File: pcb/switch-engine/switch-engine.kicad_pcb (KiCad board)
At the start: 10 copper layers, 135 x 111 mm, 369 parts, among them J1 CONN_PCIE_PWR_8PIN, J10 CORTEX_DEBUG_ETM, J11 SMPM, J12 CONN_01X03, J13 PMOD_HOST, J14 ARF6-08-S-D-A-K-TR, J15 ARF6-08-S-D-A-K-TR, J16 CONN_01X10, J17 ARF6-08-S-D-A-K-TR, J18 ARF6-08-S-D-A-K-TR, J19 CONN_01X10, J2 CONN_IBC_MGMT, J20 0826-1G1T-23-F, J21 ARF6-08-S-D-A-K-TR, J22 ARF6-08-S-D-A-K-TR, J23 CONN_01X10, J24 SMPM, J26 RJ45, J3 CONN_01X03, J4 CORTEX_DEBUG_ETM, J5 FAN_01, J6 FAN_01, J7 JUMPER_0402, J8 XILINX_JTAG, J9 PMOD_HOST, M1 SCREWHOLE, M2 SCREWHOLE, M3 SCREWHOLE, M4 SCREWHOLE, M5 LOGO, M6 LOGO, M7 LOGO, M8 960-27-23-D-AB-0, M9 FAN, Q2 SSM6N58NU, SW1 SWITCH, SW2 SWITCH, U1 STM32L431-QFN48, U10 74LVC1T45, U11 74LVC1T45, U12 74LVC1T45, U13 MT25QU256ABA8E12-0AUT, U14 ECS-1612MV-250-CN, U15 SIT9121AI-2BF-XXS156.250000G, U17 AT24MAC402, U18 74LVC1T45, U19 74LVC1T45, U2 MYMGK1R812ERSR, U20 74LVC1T45, U21 74LVC1T45, U22 ECS-1612MV-250-CN, U23 KSZ9031RN, U24 ESD224DQAR, U25 SIT9121AI-2BF-XXS156.250000G, U26 ESD224DQAR, U27 SIT9121AI-2BF-XXS156.250000G, U28 ADP1740ACPZ-2.5-R7, U29 ADM3101E_QFN, U3 MYMGK1R812ERSR, U4 MYMGK00506ERSR, U5 MYMGK00504ERSR, U6 MYMGK00504ERSR, U7 ADP1740ACPZ-1.8-R7, U8 XCKU5P-2FFVB676I, U9 STM32H735-UFBGA176-25

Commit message: Lots of routing cleanup around MCU
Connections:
- U8 pad A12: /MCU/FMC_AD8 -> /MCU/FMC_AD12
- U8 pad A13: /MCU/FMC_AD13 -> /MCU/FMC_AD10
- U8 pad A14: /MCU/FMC_AD10 -> /MCU/FMC_A17
- U8 pad B12: /MCU/FMC_AD12 -> /MCU/FMC_AD13
- U8 pad B14: /MCU/FMC_AD14 -> /MCU/FMC_A16
- U8 pad C11: /MCU/FMC_AD1 -> /MCU/FMC_AD8
- U8 pad C12: /MCU/FMC_AD11 -> /MCU/FMC_AD2
- U8 pad C13: /MCU/FMC_NE1 -> /MCU/FMC_AD14
- U8 pad C14: /MCU/FMC_AD15 -> /MCU/FMC_A18
- U8 pad C21: /RGMII PHY/ETH_LED2_N_1V8_INV -> /RGMII PHY/ETH_LED1_N_1V8_INV
- U8 pad C23: /RGMII PHY/RGMII_TXD0 -> /RGMII PHY/ETH_LED2_N_1V8_INV
- U8 pad C9: /MCU/FMC_A16 -> /MCU/FMC_NWE
- U8 pad D10: /MCU/FMC_AD0 -> /MCU/FMC_AD11
- U8 pad D11: /MCU/FMC_NE3 -> /MCU/FMC_A24
- U8 pad D13: /MCU/FMC_AD2 -> /MCU/FMC_AD0
- U8 pad D9: /MCU/FMC_A17 -> /MCU/FMC_NE2
- U8 pad E10: /MCU/FMC_A18 -> /MCU/FMC_AD15
- U8 pad E11: /MCU/FMC_NWE -> /MCU/FMC_A25
- U8 pad E12: /MCU/FMC_A24 -> /MCU/FMC_AD1
- U8 pad E13: /MCU/FMC_NWAIT -> /MCU/FMC_NE3
- U8 pad E21: /RGMII PHY/ETH_LED1_N_1V8_INV -> /RGMII PHY/ETH_LED2_N_1V8
- U8 pad F10: /MCU/FMC_NBL1 -> /MCU/FMC_A21
- U8 pad F12: /MCU/FMC_NE2 -> /MCU/FPGA_PMOD_DQ0
- U8 pad F13: /MCU/FMC_A25 -> /MCU/FMC_NWAIT
- U8 pad F14: /MCU/FMC_NL_NADV -> /MCU/FMC_NE1
- U8 pad G11: /MCU/FMC_A19 -> /MCU/FMC_AD3
- U8 pad G12: /MCU/FMC_A20 -> /MCU/FPGA_PMOD_DQ4
- U8 pad G14: /MCU/FMC_A21 -> /MCU/FMC_NL_NADV
- U8 pad G21: /RGMII PHY/ETH_LED2_N_1V8 -> /RGMII PHY/RGMII_TXD0
- U8 pad G9: /MCU/FMC_AD3 -> /MCU/FMC_A22
- U8 pad H11: /MCU/FPGA_PMOD_DQ4 -> /MCU/FMC_NBL1
- U8 pad H12: /MCU/FPGA_PMOD_DQ5 -> /MCU/FPGA_PMOD_DQ1
- U8 pad H13: /MCU/FPGA_PMOD_DQ6 -> /MCU/FPGA_PMOD_DQ2
- U8 pad J11: /MCU/FPGA_PMOD_DQ1 -> /MCU/FMC_A20
- U8 pad J12: /MCU/FPGA_PMOD_DQ2 -> /MCU/FPGA_PMOD_DQ5
- U8 pad J13: /MCU/FPGA_PMOD_DQ3 -> /MCU/FPGA_PMOD_DQ6
- U8 pad J14: /MCU/FPGA_PMOD_DQ7 -> /MCU/FPGA_PMOD_DQ3
- U8 pad J15: /MCU/FMC_A22 -> /MCU/FPGA_PMOD_DQ7
- U8 pad K10: /MCU/FPGA_PMOD_DQ0 -> /MCU/FMC_A19
- U9 pad H3: /MCU/MCU_READY -> unconnected-(U9F-PF5-PadH3)
- U9 pad N14: unconnected-(U9H-PH10-PadN14) -> /MCU/MCU_READY
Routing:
- net /MCU/3V3_SB: track 0.00 -> 174.5 mm
- net /MCU/MCU_RST_N: track 17.1 -> 113.8 mm
- net /Power Supply/12V0: track 17.6 -> 93.8 mm, vias 0 -> 3
- net /MCU/MGMT_I2C_SCL: track 0.00 -> 64.5 mm, vias 0 -> 1
- net /MCU/MGMT_I2C_SDA: track 0.00 -> 64.3 mm, vias 0 -> 1
- net /Power Supply/FAN2_PWM: track 1.52 -> 61.9 mm, vias 0 -> 1
- net /Power Supply/FAN1_PWM: track 1.55 -> 59.7 mm, vias 0 -> 1
- net /MCU/SFP0_SCL: track 9.84 -> 64.9 mm, vias 0 -> 1
- net /Power Supply/FAN2_TACH: track 2.55 -> 55.1 mm, vias 0 -> 1
- net /MCU/MCU_READY: track 0.00 -> 51.8 mm
- net /MCU/SFP0_SDA: track 11.4 -> 60.8 mm, vias 0 -> 1
- net /Power Supply/FAN1_TACH: track 2.33 -> 50.9 mm, vias 0 -> 1
- net /MCU/FMC_A22: track 75.1 -> 30.3 mm
- net /MCU/FMC_A21: track 73.0 -> 30.5 mm
- net /MCU/FMC_A20: track 68.7 -> 37.2 mm
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
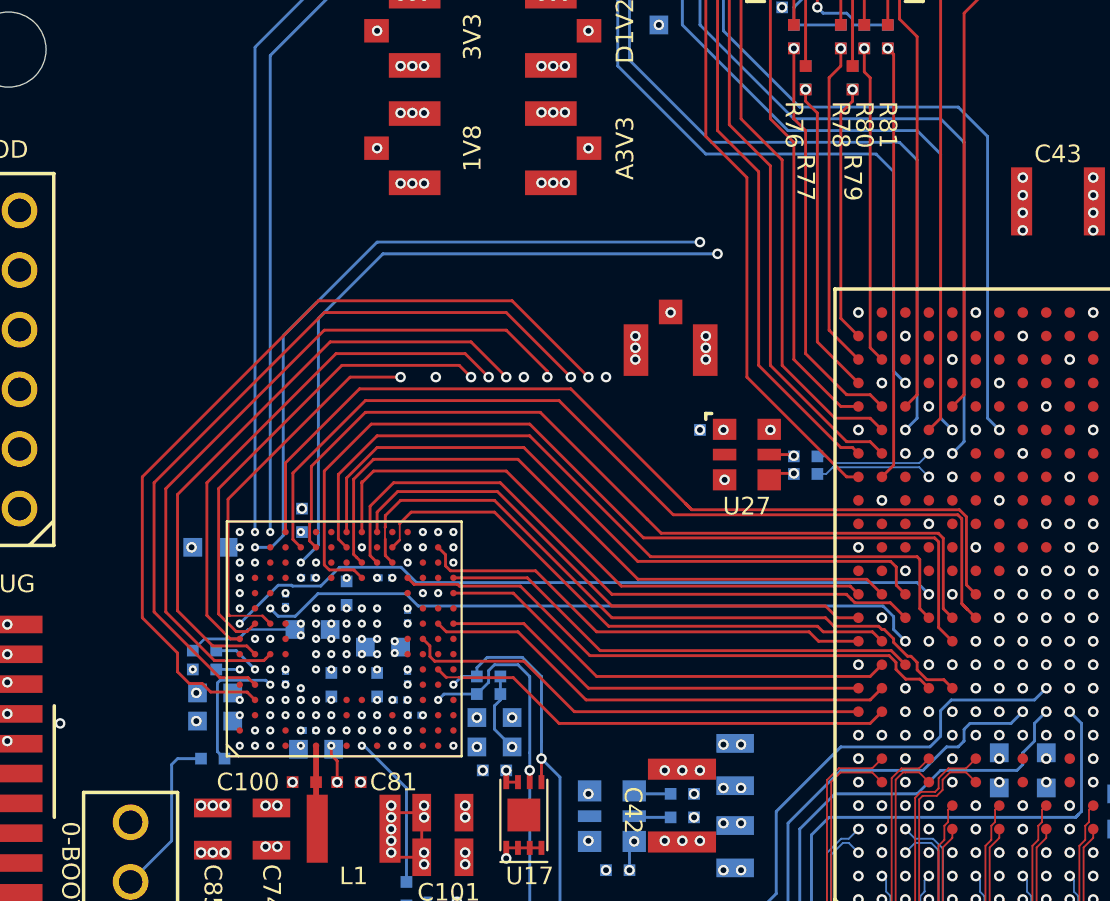
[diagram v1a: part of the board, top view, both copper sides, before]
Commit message: Rerouted FMC to not need any mid-span vias
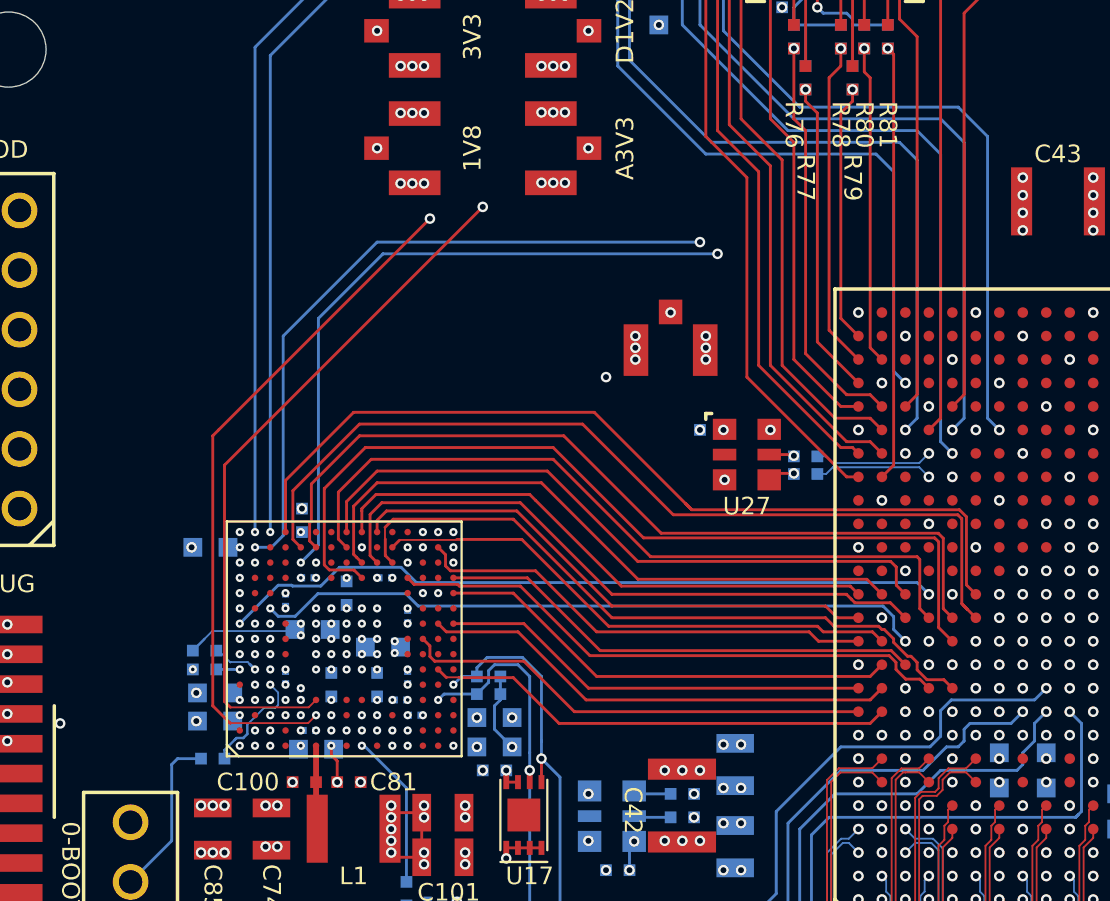
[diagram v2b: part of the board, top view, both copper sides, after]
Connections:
- U8 pad C9: /MCU/FMC_NWE -> /MCU/FMC_A22
- U8 pad D11: /MCU/FMC_A24 -> /MCU/FMC_NE2
- U8 pad D9: /MCU/FMC_NE2 -> /MCU/FMC_A21
- U8 pad E11: /MCU/FMC_A25 -> /MCU/FMC_NL_NADV
- U8 pad F10: /MCU/FMC_A21 -> /MCU/FMC_NBL1
- U8 pad F9: /MCU/FMC_NOE -> /MCU/FMC_A23
- U8 pad G10: /MCU/FMC_A23 -> /MCU/FMC_A24
- U8 pad G11: /MCU/FMC_AD3 -> /MCU/FMC_NWE
- U8 pad G14: /MCU/FMC_NL_NADV -> /MCU/FMC_A25
- U8 pad G9: /MCU/FMC_A22 -> /MCU/FMC_A20
- U8 pad H11: /MCU/FMC_NBL1 -> /MCU/FMC_AD3
- U8 pad J11: /MCU/FMC_A20 -> /MCU/FMC_NOE
- U9 pad A7: unconnected-(U9G-PG11-PadA7) -> /MCU/MCU_LED_1
- U9 pad C8: /MCU/MCU_LED_1 -> unconnected-(U9G-PG10-PadC8)
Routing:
- net /MCU/FMC_NL_NADV: track 59.0 -> 30.1 mm
- net /MCU/FMC_NBL0: track 62.5 -> 37.3 mm
- net /MCU/FMC_A25: track 57.3 -> 32.4 mm
- net /MCU/FMC_A24: track 53.4 -> 32.6 mm
- net /MCU/FMC_NE2: track 49.4 -> 30.4 mm
- net /MCU/FMC_NWE: track 47.8 -> 32.9 mm
- net /MCU/FMC_NOE: track 47.7 -> 34.7 mm
- net /Power Supply/FAN2_PWM: track 61.9 -> 53.7 mm
- net /Power Supply/FAN1_PWM: track 59.7 -> 52.7 mm
- net /MCU/SFP0_SCL: track 64.9 -> 58.1 mm
- net /Power Supply/FAN2_TACH: track 55.1 -> 48.3 mm
- net /MCU/MCU_READY: track 51.8 -> 45.4 mm
- net /Power Supply/FAN1_TACH: track 50.9 -> 44.8 mm
- net /MCU/SFP0_SDA: track 60.8 -> 54.9 mm
- net /MCU/FMC_A22: track 30.3 -> 26.0 mm
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
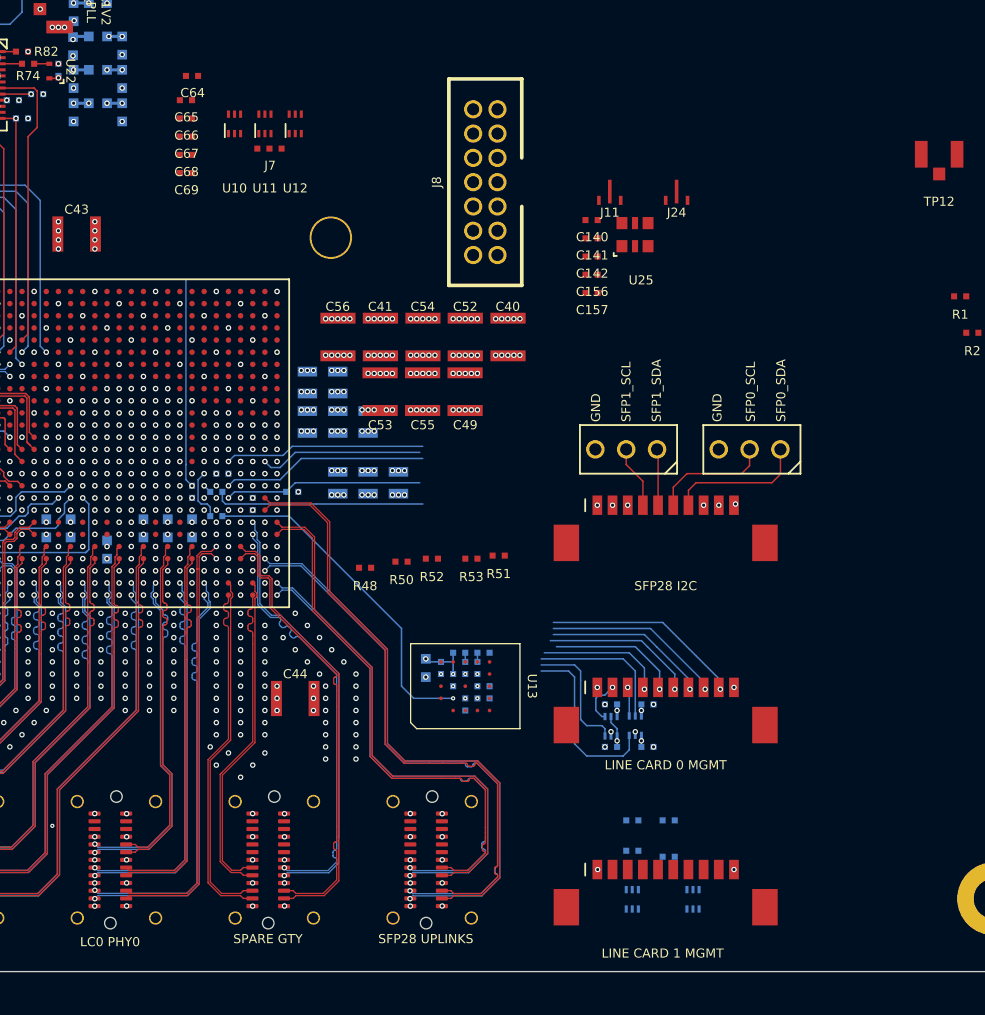
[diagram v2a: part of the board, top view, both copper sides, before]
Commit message: Routing mostly in southeast corner
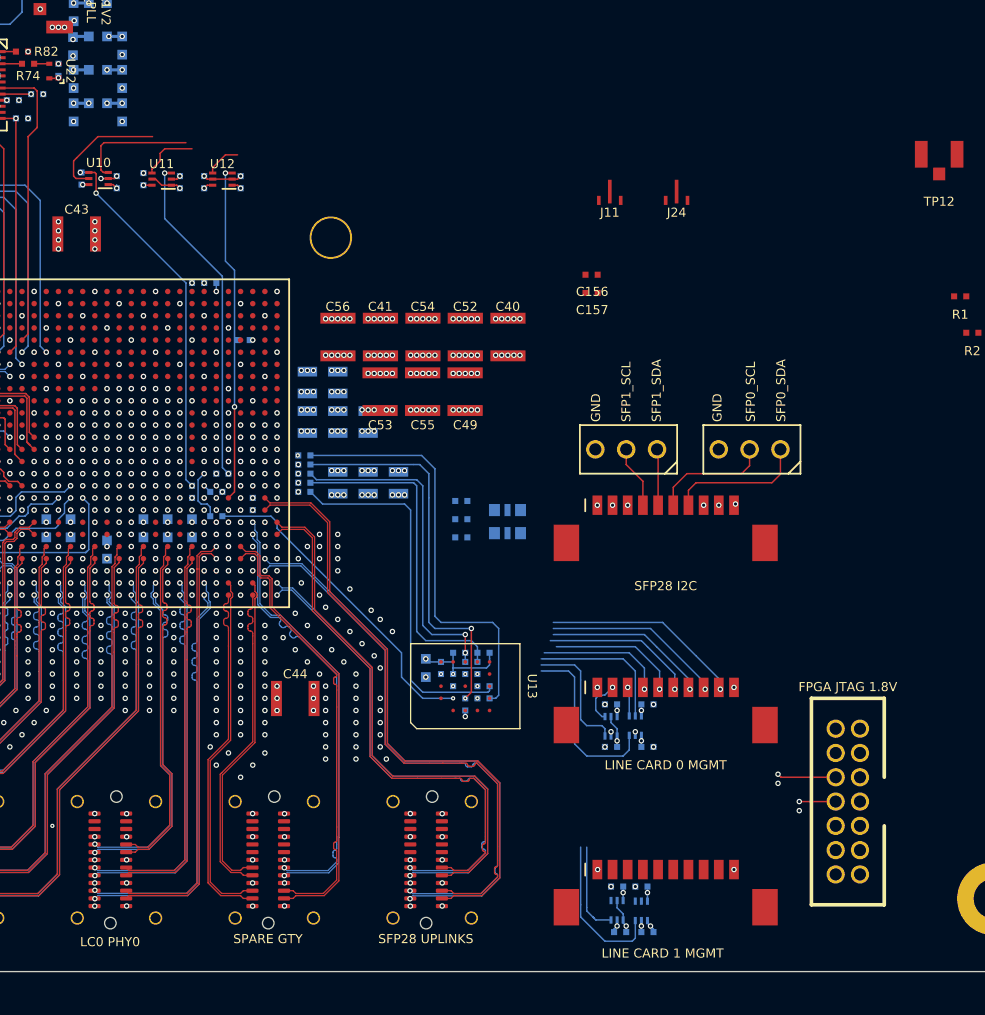
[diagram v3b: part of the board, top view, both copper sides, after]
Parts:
- C140, C141, C142, C64, C65, C66, C67, C68, C69, J7, R48, R50, R51, R52, R53, U25: moved to B.Cu
- moved J8 59.1 mm to (155.0, 128.0)
- moved U25 25.9 mm to (127.0, 105.0), turned to 180 degrees
- moved C140 25.5 mm to (123.2, 103.2), turned to 180 degrees
- moved C141 25.5 mm to (123.2, 104.8), turned to 180 degrees
- moved C142 25.5 mm to (123.2, 106.2), turned to 180 degrees
- moved R51 18.0 mm to (110.2, 99.5)
- moved R53 15.1 mm to (110.2, 101.8)
- moved R41 13.1 mm to (105.2, 90.0)
- moved R52 12.6 mm to (110.2, 101.0)
- moved C64 12.4 mm to (91.9, 76.7), turned to 90 degrees
- moved J7 12.3 mm to (102.0, 85.3)
- moved U10 12.1 mm to (93.3, 76.7), turned to 90 degrees
- moved C105 10.0 mm to (136.2, 138.8)
- moved R48 9.86 mm to (110.3, 100.2)
- moved R50 9.85 mm to (110.2, 102.5)
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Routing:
- net /GND: track 1635.9 -> 1732.8 mm, vias 706 -> 746
- net /1V8: track 262.4 -> 326.6 mm, vias 54 -> 57
- net /FPGA support/FPGA_JTAG_TMS: track 16.9 -> 75.4 mm
- net /FPGA support/FPGA_JTAG_TCK: track 13.5 -> 68.2 mm
- net /FPGA support/FPGA_JTAG_TDI: track 16.5 -> 70.9 mm, vias 1 -> 2
- net /FPGA support/FPGA_JTAG_TDO: track 17.4 -> 69.1 mm, vias 0 -> 2
- net /3V3: track 474.7 -> 513.4 mm, vias 65 -> 70
- net /FPGA support/FPGA_FLASH_DQ1: track 0.00 -> 34.9 mm
- net /FPGA support/FPGA_FLASH_CS_N: track 0.00 -> 32.0 mm, vias 1 -> 2
- net /FPGA support/FPGA_FLASH_DQ0: track 0.00 -> 30.2 mm
- net /FPGA support/FPGA_FLASH_DQ3: track 0.75 -> 27.6 mm
- net /FPGA support/FPGA_FLASH_DQ2: track 0.75 -> 27.2 mm, vias 0 -> 2
- net /FPGA support/FPGA_DONE: track 5.55 -> 27.5 mm, vias 1 -> 2
- net /Line card interfaces/LC1_MDIO_3V3: track 0.00 -> 21.3 mm
- net /2V5: track 3.95 -> 23.5 mm, vias 2 -> 4
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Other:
- board text added: "FPGA JTAG 1.8V"

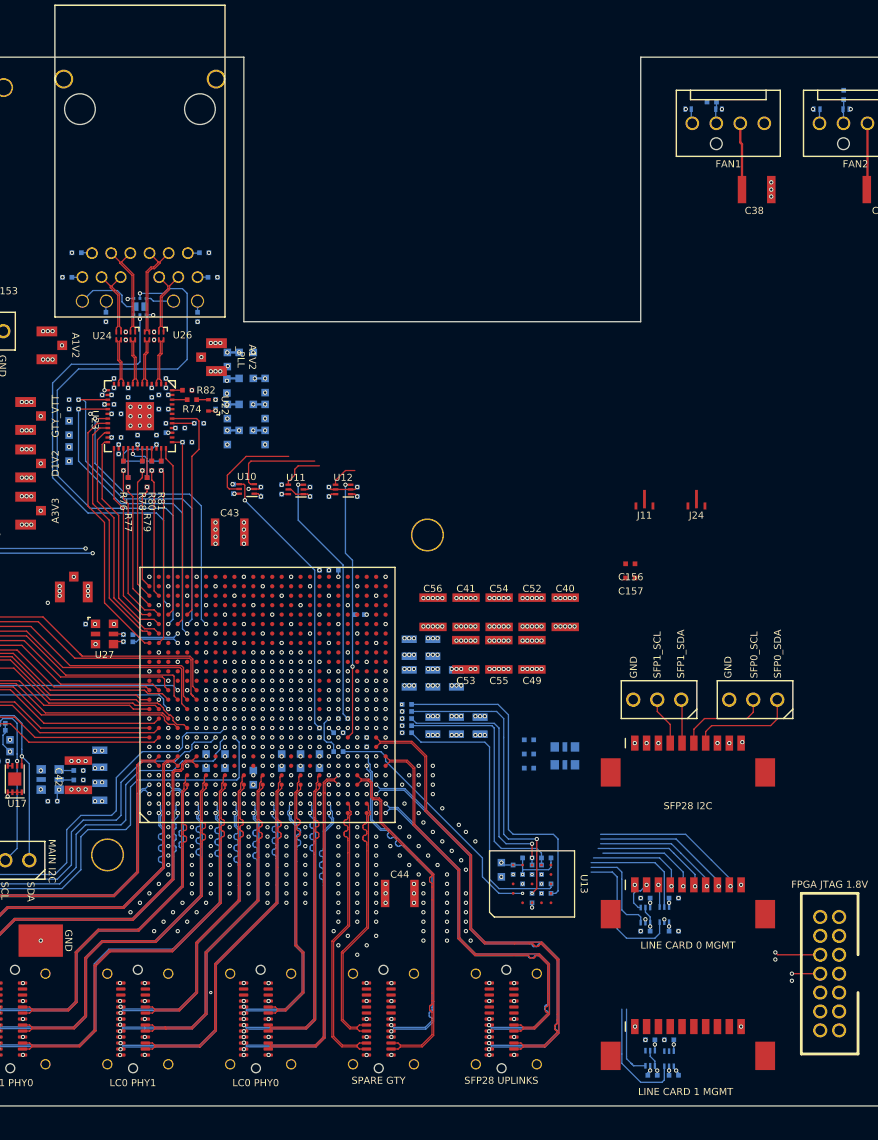
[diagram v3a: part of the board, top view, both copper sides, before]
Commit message: Routed line card management low-speed signals
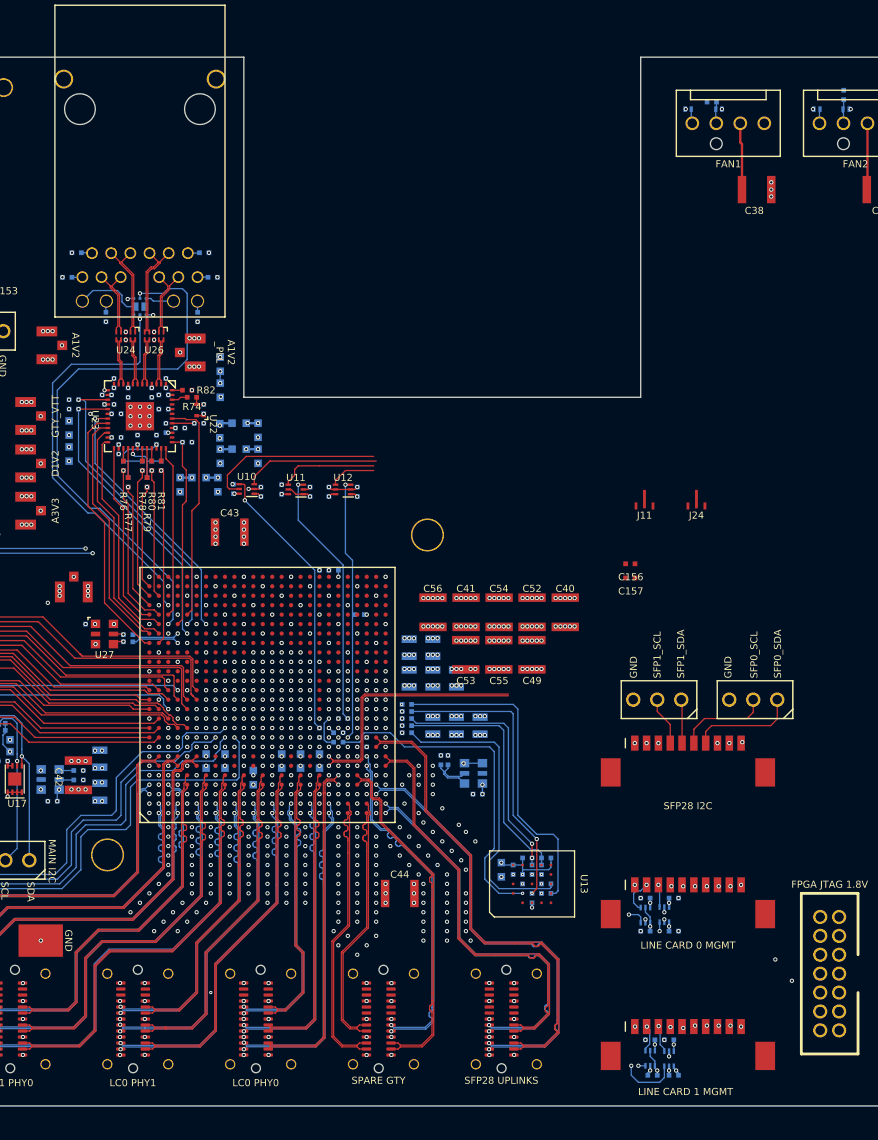
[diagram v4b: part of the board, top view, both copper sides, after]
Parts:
- moved U25 9.85 mm to (117.3, 106.8), turned to -90 degrees
- moved C142 9.36 mm to (113.8, 105.4), turned to 90 degrees
- moved C141 8.60 mm to (114.6, 105.4), turned to 90 degrees
- moved M9 8.50 mm to (114.0, 56.5)
- moved C140 7.91 mm to (117.8, 109.0), turned to 0 degrees
- moved C113 7.07 mm to (90.2, 76.2)
- moved C124 7.07 mm to (86.2, 76.2)
- moved FB5 7.07 mm to (88.2, 75.5)
- moved C112 4.80 mm to (94.5, 73.2)
- moved C115 4.80 mm to (94.5, 70.5)
- moved C123 4.80 mm to (90.5, 73.2)
- moved C125 4.80 mm to (90.5, 70.5)
- moved FB4 4.80 mm to (92.5, 72.5)
- moved FB6 4.80 mm to (92.5, 69.7)
- moved C126 3.34 mm to (90.5, 66.2)
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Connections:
- C141 pad 1: /SFP28 interfaces/RC2_P -> /SFP28 interfaces/RC2_N
- C142 pad 1: /SFP28 interfaces/RC2_N -> /SFP28 interfaces/RC2_P
- U8 pad AA13: /Line card interfaces/LC0_SPI_CS_N -> /Line card interfaces/LC1_MDC_3V3
- U8 pad AA14: /Line card interfaces/LC1_SPI_SCK -> /Line card interfaces/LC1_I2C_SCL
- U8 pad AA15: /Line card interfaces/LC1_SPI_MISO -> /Line card interfaces/LC1_I2C_SDA
- U8 pad AB14: /Line card interfaces/LC1_SPI_CS_N -> /Line card interfaces/LC0_SPI_MOSI
- U8 pad AB15: /Line card interfaces/LC1_MDC_3V3 -> /Line card interfaces/LC1_MDIO_OE
- U8 pad AB16: /Line card interfaces/LC0_MDC_3V3 -> /Line card interfaces/LC1_SPI_SCK
- U8 pad AC13: /Line card interfaces/LC1_MDIO_3V3 -> /Line card interfaces/LC0_MDC_3V3
- U8 pad AC14: /Line card interfaces/LC0_MDIO_3V3 -> /Line card interfaces/LC0_SPI_MISO
- U8 pad AD13: /Line card interfaces/LC1_MDIO_OE -> /Line card interfaces/LC1_SPI_MISO
- U8 pad AD15: /Line card interfaces/LC1_I2C_SCL -> /Line card interfaces/LC0_SPI_SCK
- U8 pad AE13: /Line card interfaces/LC0_SPI_MOSI -> /Line card interfaces/LC1_SPI_MOSI
- U8 pad AE15: /Line card interfaces/LC0_SPI_MISO -> /Line card interfaces/LC0_SPI_CS_N
- U8 pad AF13: /Line card interfaces/LC1_SPI_MOSI -> /Line card interfaces/LC0_MDIO_3V3
- U8 pad AF14: /Line card interfaces/LC0_I2C_SDA -> /Line card interfaces/LC0_I2C_SCL
- U8 pad AF15: /Line card interfaces/LC0_I2C_SCL -> /Line card interfaces/LC0_I2C_SDA
- U8 pad Y13: /Line card interfaces/LC0_SPI_SCK -> /Line card interfaces/LC1_MDIO_3V3
- U8 pad Y16: /Line card interfaces/LC1_I2C_SDA -> /Line card interfaces/LC1_SPI_CS_N
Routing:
- net /Line card interfaces/LC1_MDIO_OE: track 5.27 -> 73.2 mm, vias 1 -> 2
- net /Line card interfaces/LC1_SPI_SCK: track 8.46 -> 68.6 mm, vias 1 -> 2
- net /Line card interfaces/LC1_SPI_CS_N: track 11.1 -> 70.2 mm, vias 1 -> 2
- net /Line card interfaces/LC1_SPI_MOSI: track 4.82 -> 62.7 mm, vias 1 -> 2
- net /Line card interfaces/LC1_I2C_SCL: track 9.01 -> 66.3 mm, vias 1 -> 2
- net /Line card interfaces/LC1_I2C_SDA: track 12.8 -> 68.3 mm, vias 1 -> 2
- net /Line card interfaces/LC1_MDIO_3V3: track 21.3 -> 73.3 mm, vias 1 -> 2
- net /Line card interfaces/LC1_SPI_MISO: track 12.0 -> 63.0 mm, vias 1 -> 2
- net /Line card interfaces/LC1_MDC_3V3: track 18.8 -> 67.6 mm, vias 1 -> 2
- net /Line card interfaces/LC0_SPI_MOSI: track 21.9 -> 59.6 mm
- net /Line card interfaces/LC0_SPI_MISO: track 23.0 -> 57.2 mm
- net /Line card interfaces/LC0_MDIO_OE: track 19.8 -> 52.0 mm, vias 1 -> 2
- net /Line card interfaces/LC0_MDC_3V3: track 21.1 -> 50.6 mm, vias 1 -> 2
- net /Line card interfaces/LC0_I2C_SDA: track 17.0 -> 46.6 mm
- net /Line card interfaces/LC0_SPI_SCK: track 23.1 -> 51.7 mm
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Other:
- outline, holes or cut-outs redrawn
- board text added: "Chassis lip"
